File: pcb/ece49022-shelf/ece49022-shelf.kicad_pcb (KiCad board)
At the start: 4 copper layers, 44.2 x 53.6 mm, 77 parts, among them IC1 NAU7802, J1 USB_B_Micro, J2 Conn_01x16_Pin, J3 Conn_01x04_Pin, J4 Conn_01x03_Pin, J5 Conn_02x03_Counter_Clockwise, J6 Conn_01x03_Pin, J7 Conn_01x02_Pin, J8 Conn_02x03_Counter_Clockwise, SW1 SW_Push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

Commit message: shelf is ready
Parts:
- added D3: LED, Resistor_SMD:R_0603_1608Metric, F.Cu at (196.0, 91.5)
- added D4: LED, Resistor_SMD:R_0603_1608Metric, F.Cu at (190.9, 91.5)
- added R21: 100, Resistor_SMD:R_0603_1608Metric, F.Cu at (194.4, 91.5)
- added R22: 100, Resistor_SMD:R_0603_1608Metric, F.Cu at (189.3, 91.5)
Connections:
- C32 pad 1: +5V -> +3V3
- IC1 pad 15: +5V -> +3V3
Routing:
- net +5V: track 88.3 -> 67.3 mm, vias 5 -> 3
- net /5V_USB: track 8.39 -> 11.9 mm
- net /Power/5V_SREG: track 31.2 -> 34.7 mm
- net +3V3: track 23.1 -> 26.0 mm
- net GND: track 41.3 -> 44.1 mm, vias 131 -> 119
- net Net-(D4-A): track 0.00 -> 1.62 mm
- net Net-(D3-A): track 0.00 -> 1.60 mm
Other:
- board text added: "LED"
- board text added: "NAU7802 5V pull ups Review Return Current Paths Additional LED for SREG and USB power"
- board text removed: "21"

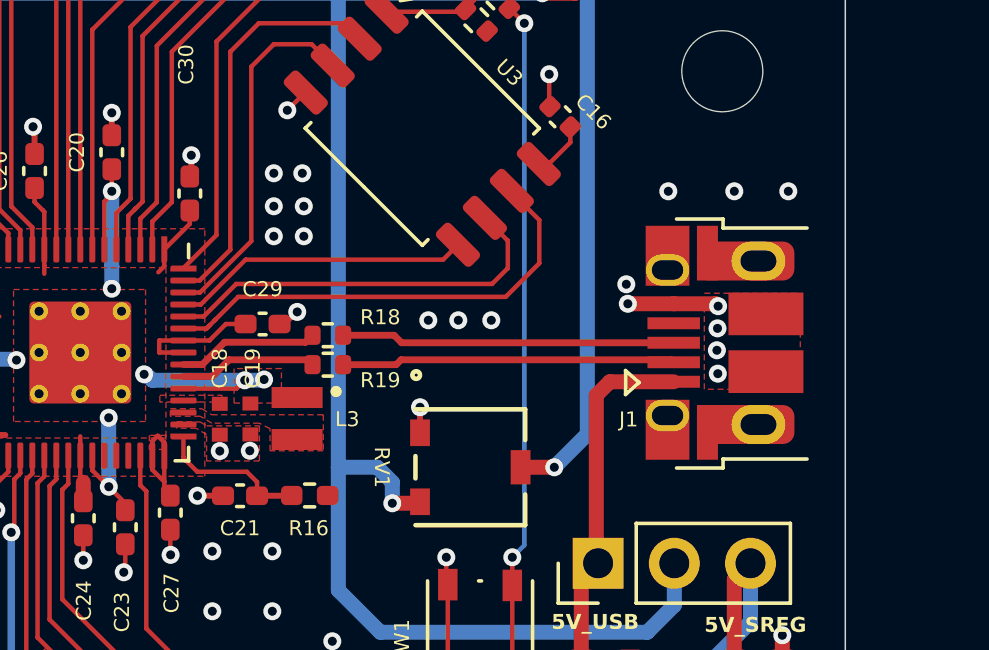
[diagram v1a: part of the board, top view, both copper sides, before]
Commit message: fixed some stuff in interface and changed trace width for 50 ohm in shelf pcb
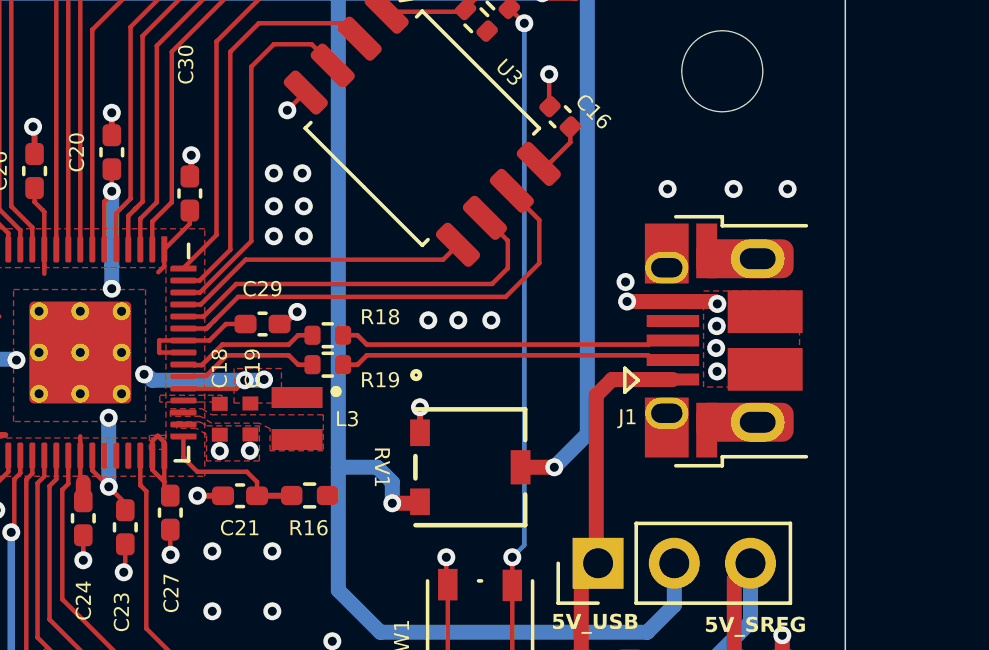
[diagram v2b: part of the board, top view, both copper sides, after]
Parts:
- R11: value R_Small_US -> 100
- moved J1 0.08 mm to (195.2, 80.0)
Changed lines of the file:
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@@
 			(plot_on_all_layers_selection 0x00000000_00000000_00000000_00000000)
 			(disableapertmacros no)
-			(usegerberextensions no)
+			(usegerberextensions yes)
 			(usegerberattributes yes)
 			(usegerberadvancedattributes yes)
-			(creategerberjobfile yes)
+			(creategerberjobfile no)
 			(dashed_line_dash_ratio 12.000000)
 			(dashed_line_gap_ratio 3.000000)
@@
 			(outputformat 1)
 			(mirror no)
-			(drillshape 1)
+			(drillshape 0)
 			(scaleselection 1)
-			(outputdirectory "")
+			(outputdirectory "../shelf-gerbers/")
 		)
 	)
@@
 	(footprint "49022_Footprints:USB_Micro-B_Amphenol_10103594-0001LF_Horizontal_modified"
 		(layer "F.Cu")
-		(at 195.2046 80.0504 90)
+		(at 195.18 79.975 90)
 		(descr "Micro USB Type B 10103594-0001LF, http://cdn.amphenol-icc.com/media/wysiwyg/files/drawing/10103594.pdf")
 		(tags "USB USB_B USB_micro USB_OTG")
@@
 			)
 		)
-		(property "Value" "R_Small_US"
+		(property "Value" "100"
 			(at 0 1.65 135)
 			(layer "F.Fab")
@@
 	)
 	(segment
-		(start 192.3796 78.7504)
-		(end 190.8504 78.7504)
+		(start 192.355 78.675)
+		(end 190.8258 78.675)
 		(width 0.5)
 		(layer "F.Cu")
@@
 	)
 	(segment
-		(start 193.7804 78.7504)
-		(end 193.86 78.83)
+		(start 193.7558 78.675)
+		(end 193.8354 78.7546)
 		(width 0.5)
 		(layer "F.Cu")
@@
 	)
 	(segment
-		(start 192.3796 78.7504)
-		(end 193.7804 78.7504)
+		(start 192.355 78.675)
+		(end 193.7558 78.675)
 		(width 0.5)
 		(layer "F.Cu")
@@
 	)
 	(via
-		(at 190.8 78.1)
+		(at 190.7754 78.0246)
 		(size 0.6)
 		(drill 0.3)
@@
 	)
 	(via
-		(at 193.86 78.83)
+		(at 193.8354 78.7546)
 		(size 0.6)
 		(drill 0.3)
@@
 	)
 	(via
-		(at 196.2 75)
+		(at 196.1754 74.9246)
 		(size 0.6)
 		(drill 0.3)
@@
 	)
 	(via
-		(at 193.84 79.57)
+		(at 193.8154 79.4946)
 		(size 0.6)
 		(drill 0.3)
@@
 	)
 	(via
-		(at 194.4 75)
+		(at 194.3754 74.9246)
 		(size 0.6)
 		(drill 0.3)
@@
 	)
 	(via
-		(at 190.8504 78.7504)
+		(at 190.8258 78.675)
 		(size 0.6)
 		(drill 0.3)
@@
 	)
 	(via
-		(at 193.85 81.08)
+		(at 193.8254 81.0046)
 		(size 0.6)
 		(drill 0.3)
@@
 	)
 	(via
-		(at 192.2 75)
+		(at 192.1754 74.9246)
 		(size 0.6)
 		(drill 0.3)
@@
 	)
 	(via
-		(at 193.82 80.3)
+		(at 193.7954 80.2246)
 		(size 0.6)
 		(drill 0.3)
@@
 	)
 	(segment
+		(start 191.68 79.975)
+		(end 192.355 79.975)
+		(width 0.155448)
+		(layer "F.Cu")
+		(net 24)
+	)
+	(segment
+		(start 191.544324 80.110676)
+		(end 191.68 79.975)
+		(width 0.155448)
+		(layer "F.Cu")
+		(net 24)
+	)
+	(segment
 		(start 181.36 79.8)
-		(end 183.060001 79.8)
-		(width 0.2286)
+		(end 181.840001 79.8)
+		(width 0.155448)
 		(layer "F.Cu")
 		(net 24)
 	)
 	(segment
-		(start 183.310401 80.0504)
-		(end 192.3796 80.0504)
-		(width 0.2286)
+		(start 182.150677 80.110676)
+		(end 191.544324 80.110676)
+		(width 0.155448)
 		(layer "F.Cu")
 		(net 24)
 	)
 	(segment
-		(start 183.060001 79.8)
-		(end 183.310401 80.0504)
-		(width 0.2286)
+		(start 181.840001 79.8)
+		(end 182.150677 80.110676)
+		(width 0.155448)
 		(layer "F.Cu")
 		(net 24)
 	)
 	(segment
-		(start 183.292901 80.6171)
-		(end 192.2963 80.6171)
-		(width 0.2286)
+		(start 191.68 80.625)
+		(end 192.355 80.625)
+		(width 0.155448)
 		(layer "F.Cu")
 		(net 25)
 	)
 	(segment
-		(start 183.130001 80.78)
-		(end 183.292901 80.6171)
-		(width 0.2286)
+		(start 191.524324 80.469324)
+		(end 191.68 80.625)
+		(width 0.155448)
 		(layer "F.Cu")
 		(net 25)
 	)
 	(segment
-		(start 181.36 80.78)
-		(end 183.130001 80.78)
-		(width 0.2286)
+		(start 181.840001 80.78)
+		(end 182.150677 80.469324)
+		(width 0.155448)
+		(layer "F.Cu")
+		(net 25)
+	)
+	(segment
+		(start 182.150677 80.469324)
+		(end 191.524324 80.469324)
+		(width 0.155448)
 		(layer "F.Cu")
 		(net 25)
 	)
 	(segment
-		(start 192.3292 80.65)
-		(end 192.3796 80.7004)
+		(start 192.3046 80.5746)
+		(end 192.355 80.625)
 		(width 0.14)
 		(layer "F.Cu")
@@
 	)
 	(segment
-		(start 192.2963 80.6171)
-		(end 192.3796 80.7004)
-		(width 0.2286)
+		(start 181.36 80.78)
+		(end 181.840001 80.78)
+		(width 0.155448)
 		(layer "F.Cu")
 		(net 25)
@@
 	)
 	(segment
-		(start 189.3 90.675)
-		(end 189.3 87.96)
+		(start 192.355 81.275)
+		(end 190.325 81.275)
 		(width 0.5)
 		(layer "F.Cu")
@@
 	)
 	(segment
-		(start 189.8 81.8)
-		(end 189.8 87.34)
+		(start 189.3 90.675)
+		(end 189.3 87.96)
 		(width 0.5)
 		(layer "F.Cu")
@@
 	)
 	(segment
-		(start 189.3 87.96)
-		(end 189.86 87.4)
+		(start 190.325 81.275)
+		(end 189.8 81.8)
 		(width 0.5)
 		(layer "F.Cu")
@@
 	)
 	(segment
-		(start 192.3796 81.3504)
-		(end 190.2496 81.3504)
+		(start 189.3 87.96)
+		(end 189.86 87.4)
 		(width 0.5)
 		(layer "F.Cu")
@@
 	)
 	(segment
-		(start 190.2496 81.3504)
-		(end 189.8 81.8)
+		(start 189.8 81.8)
+		(end 189.8 87.34)
 		(width 0.5)
 		(layer "F.Cu")
@@
 	)
 	(segment
-		(start 180.34 79.8)
-		(end 180.1071 80.0329)
-		(width 0.2286)
+		(start 176.0375 80.775)
+		(end 176.375 80.775)
+		(width 0.155448)
+		(layer "F.Cu")
+		(net 73)
+	)
+	(segment
+		(start 176.395676 80.795676)
+		(end 176.65072 80.795676)
+		(width 0.155448)
+		(layer "F.Cu")
+		(net 73)
+	)
+	(segment
+		(start 177.33572 80.110676)
+		(end 179.549323 80.110676)
+		(width 0.155448)
+		(layer "F.Cu")
+		(net 73)
+	)
+	(segment
+		(start 176.375 80.775)
+		(end 176.395676 80.795676)
+		(width 0.155448)
 		(layer "F.Cu")
 		(net 73)
 	)
 	(segment
-		(start 180.1071 80.0329)
-		(end 177.41 80.0329)
-		(width 0.2286)
+		(start 176.65072 80.795676)
+		(end 177.33572 80.110676)
+		(width 0.155448)
 		(layer "F.Cu")
 		(net 73)
 	)
 	(segment
-		(start 177.41 80.0329)
-		(end 176.6679 80.775)
-		(width 0.2286)
+		(start 179.859999 79.8)
+		(end 180.34 79.8)
+		(width 0.155448)
 		(layer "F.Cu")
 		(net 73)
 	)
 	(segment
-		(start 176.6679 80.775)
-		(end 176.0375 80.775)
-		(width 0.2286)
+		(start 179.549323 80.110676)
+		(end 179.859999 79.8)
+		(width 0.155448)
 		(layer "F.Cu")
 		(net 73)
 	)
 	(segment
-		(start 177.56 80.6171)
-		(end 177.0021 81.175)
-		(width 0.2286)
+		(start 179.859999 80.78)
+		(end 180.34 80.78)
+		(width 0.155448)
+		(layer "F.Cu")
+		(net 74)
+	)
+	(segment
+		(start 179.549323 80.469324)
+		(end 179.859999 80.78)
+		(width 0.155448)
+		(layer "F.Cu")
+		(net 74)
+	)
+	(segment
+		(start 177.48428 80.469324)
+		(end 179.549323 80.469324)
+		(width 0.155448)
+		(layer "F.Cu")
+		(net 74)
+	)
+	(segment
+		(start 176.395676 81.154324)
+		(end 176.79928 81.154324)
+		(width 0.155448)
 		(layer "F.Cu")
 		(net 74)
 	)
 	(segment
-		(start 180.34 80.78)
-		(end 180.1771 80.6171)
-		(width 0.2286)
+		(start 176.0375 81.175)
+		(end 176.375 81.175)
+		(width 0.155448)
 		(layer "F.Cu")
 		(net 74)
 	)
 	(segment
-		(start 180.1771 80.6171)
-		(end 177.56 80.6171)
-		(width 0.2286)
+		(start 176.79928 81.154324)
+		(end 177.48428 80.469324)
+		(width 0.155448)
 		(layer "F.Cu")
 		(net 74)
 	)
 	(segment
-		(start 177.0021 81.175)
-		(end 176.0375 81.175)
-		(width 0.2286)
+		(start 176.375 81.175)
+		(end 176.395676 81.154324)
+		(width 0.155448)
 		(layer "F.Cu")
 		(net 74)
@@
 		(polygon
 			(pts
-				(xy 193.4 78.4) (xy 196.6 78.4) (xy 196.6 81.6) (xy 193.4 81.6)
+				(xy 193.3754 78.3246) (xy 196.5754 78.3246) (xy 196.5754 81.5246) (xy 193.3754 81.5246)
 			)
 		)
